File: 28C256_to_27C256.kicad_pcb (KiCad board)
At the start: 2 copper layers, 16.4 x 34.2 mm, 4 parts, among them J1 27C256 DIP LEGS, U1 28C256

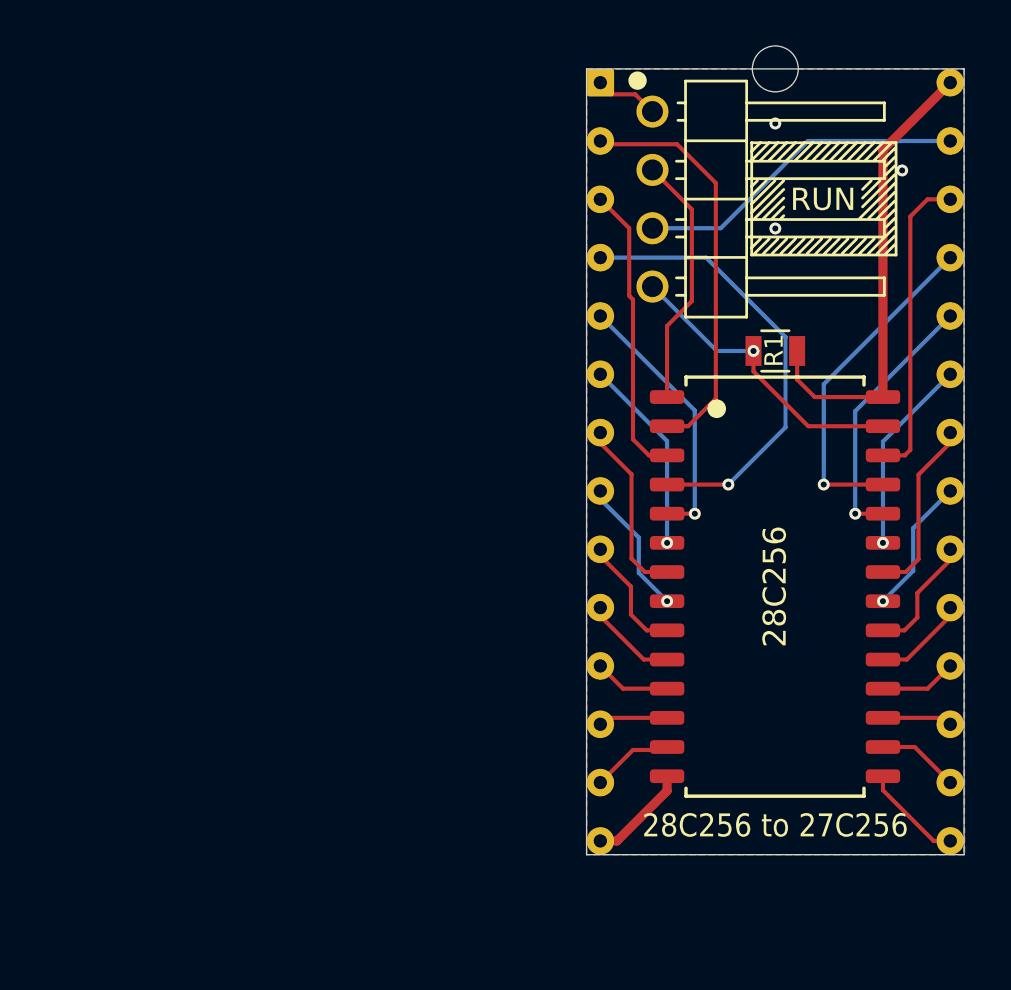
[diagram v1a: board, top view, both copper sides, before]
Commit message: simpler programming adapters, update pics and BOMs
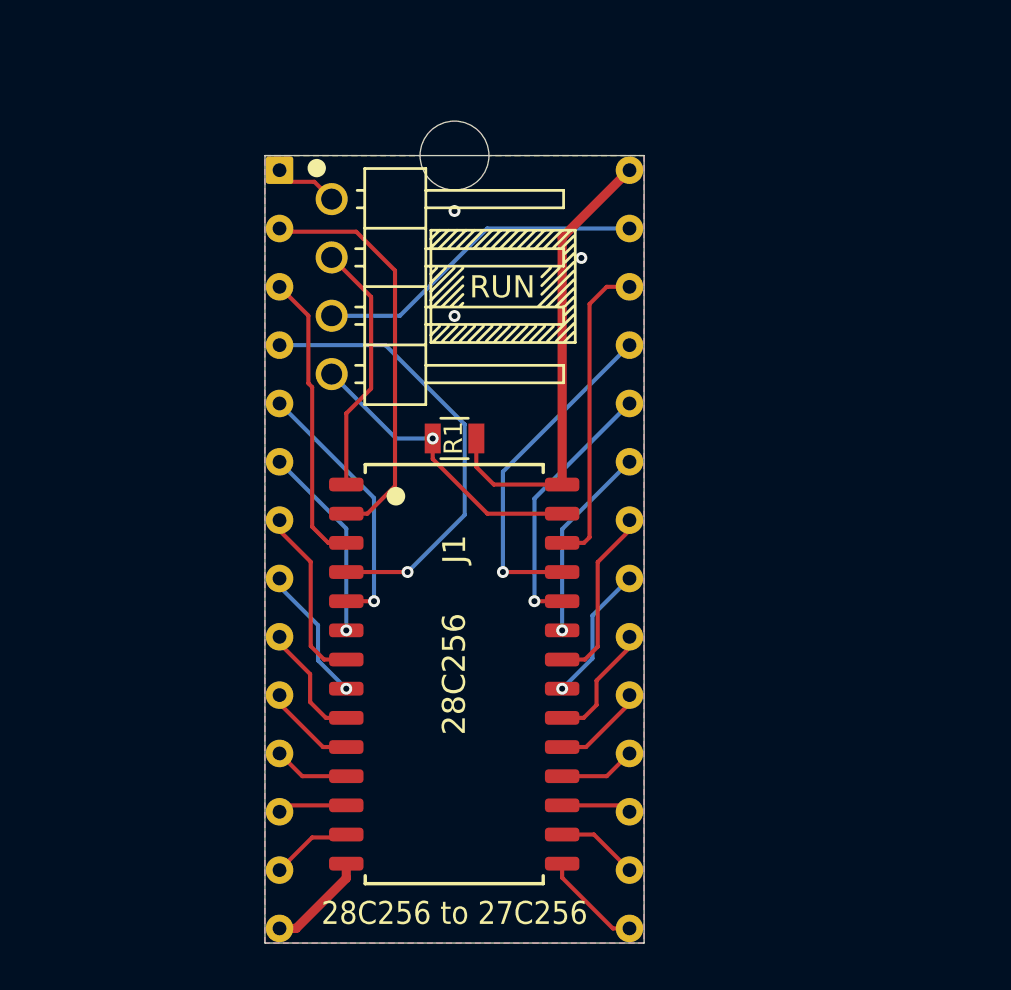
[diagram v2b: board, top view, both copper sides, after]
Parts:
- added REF**: NPTH_3mm, 000_LOCAL:NPTH_3mm, F.Cu at (136.0, 86.7)
- J1: footprint 000_LOCAL:DIP-28_W15.24mm_pcb_sil_pins -> 000_LOCAL:DIP28_0.6_pcb_sil_pins
- moved J1 14.5 mm to (136.0, 103.8)
- moved JP1 14.5 mm to (130.7, 88.6)
- moved U1 14.5 mm to (136.0, 109.2)
- moved R1 14.5 mm to (136.0, 99.0)
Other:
- board size 16.4 x 34.2 mm -> 16.5 x 34.3 mm

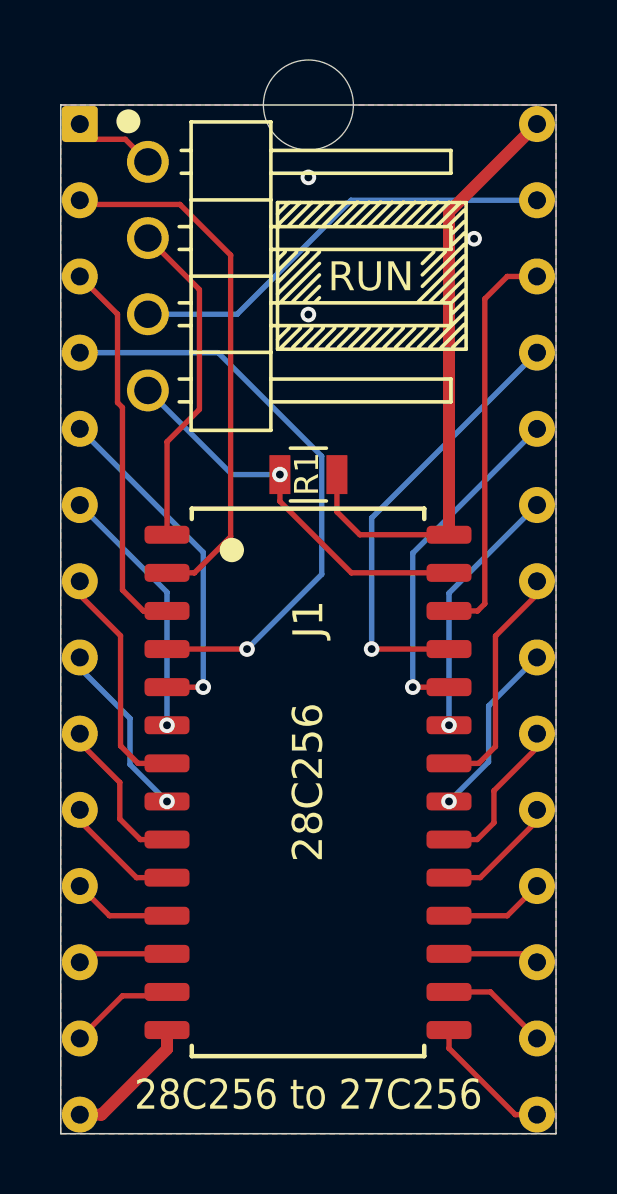
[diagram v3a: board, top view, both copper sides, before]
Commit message: 0.3mm drills, gnd zone fills
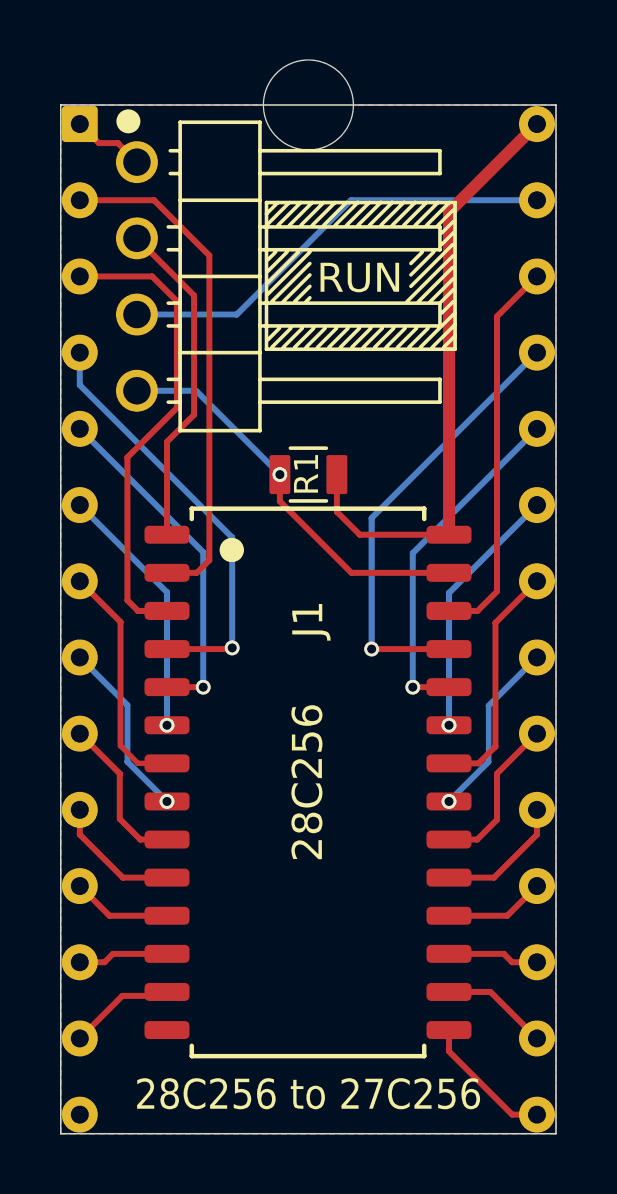
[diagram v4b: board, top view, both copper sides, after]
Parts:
- moved JP1 0.37 mm to (130.3, 88.6)
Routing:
- net /A6: track 19.6 -> 14.1 mm
- net /GND: track 4.45 -> 0.00 mm, vias 3 -> 0
- net /A7: track 12.8 -> 15.7 mm
- net /A12: track 17.8 -> 16.8 mm
- net /A13: track 13.5 -> 12.9 mm
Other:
- net class Default: trace_width 0.25 -> 0.2; via_dia 0.8 -> 0.5; via_drill 0.4 -> 0.3
- rule trace_min: 0.16 -> 0.2
- rule via_min_drill: 0.26 -> 0.3
- rule via_min_size: 0.52 -> 0.5

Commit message: make room to stow programming jumper on 28C256_to_27C256
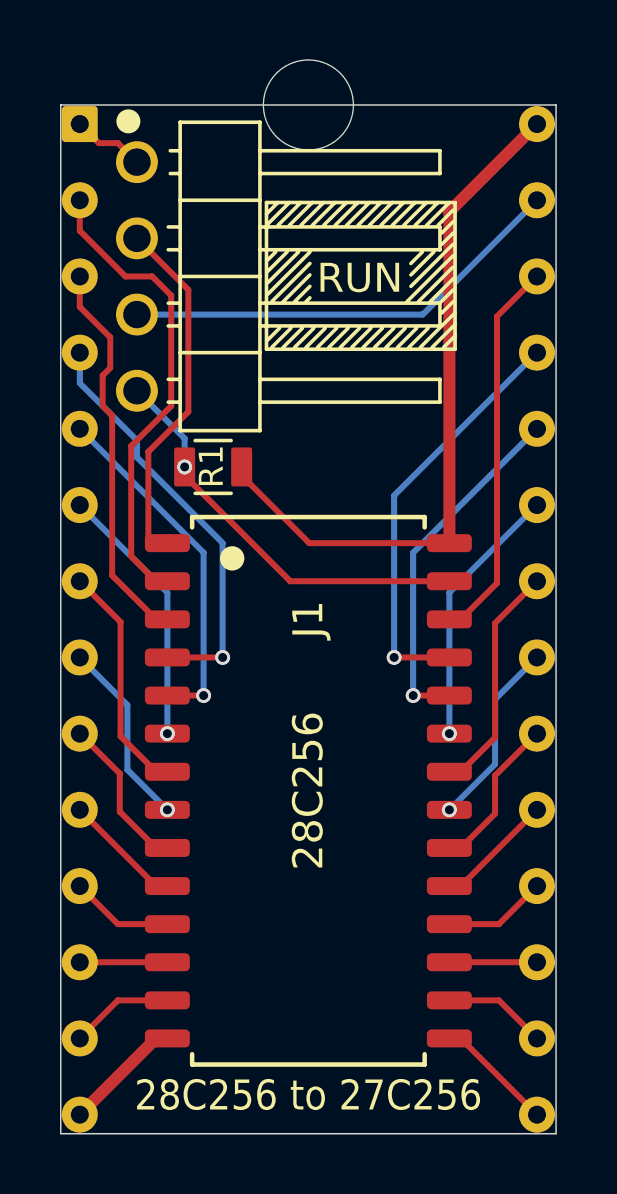
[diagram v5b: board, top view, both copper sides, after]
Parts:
- moved R1 3.19 mm to (132.9, 98.7)
- moved U1 0.28 mm to (136.0, 109.5)
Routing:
- net /GND: track 0.00 -> 3.97 mm
- net /VCC: track 20.2 -> 23.3 mm
- net /A7: track 15.7 -> 13.1 mm
- net /A12: track 16.8 -> 15.8 mm
- net /A14: track 11.0 -> 12.1 mm
- net /A8: track 14.7 -> 14.0 mm
- net /D3: track 4.52 -> 3.97 mm
- removed copper zone on B.Cu, net /GND
- removed copper zone on F.Cu, net /GND

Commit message: add DS1000_DIP14
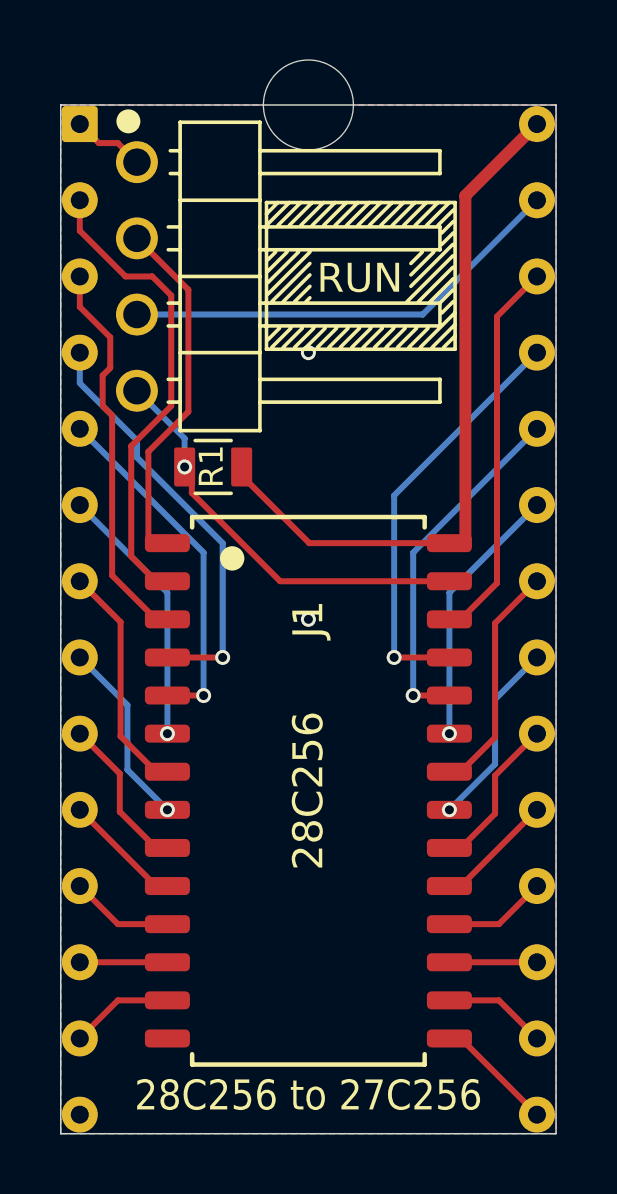
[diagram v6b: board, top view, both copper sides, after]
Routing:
- net /GND: track 3.97 -> 0.00 mm, vias 0 -> 2
- added copper zone on B.Cu, net /GND
- added copper zone on F.Cu, net /GND

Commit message: kicad 6
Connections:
- net /~CE renamed /~{CE}
- net /~OE renamed /~{OE}
- net /~WE renamed /~{WE}
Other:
- net class Default removed

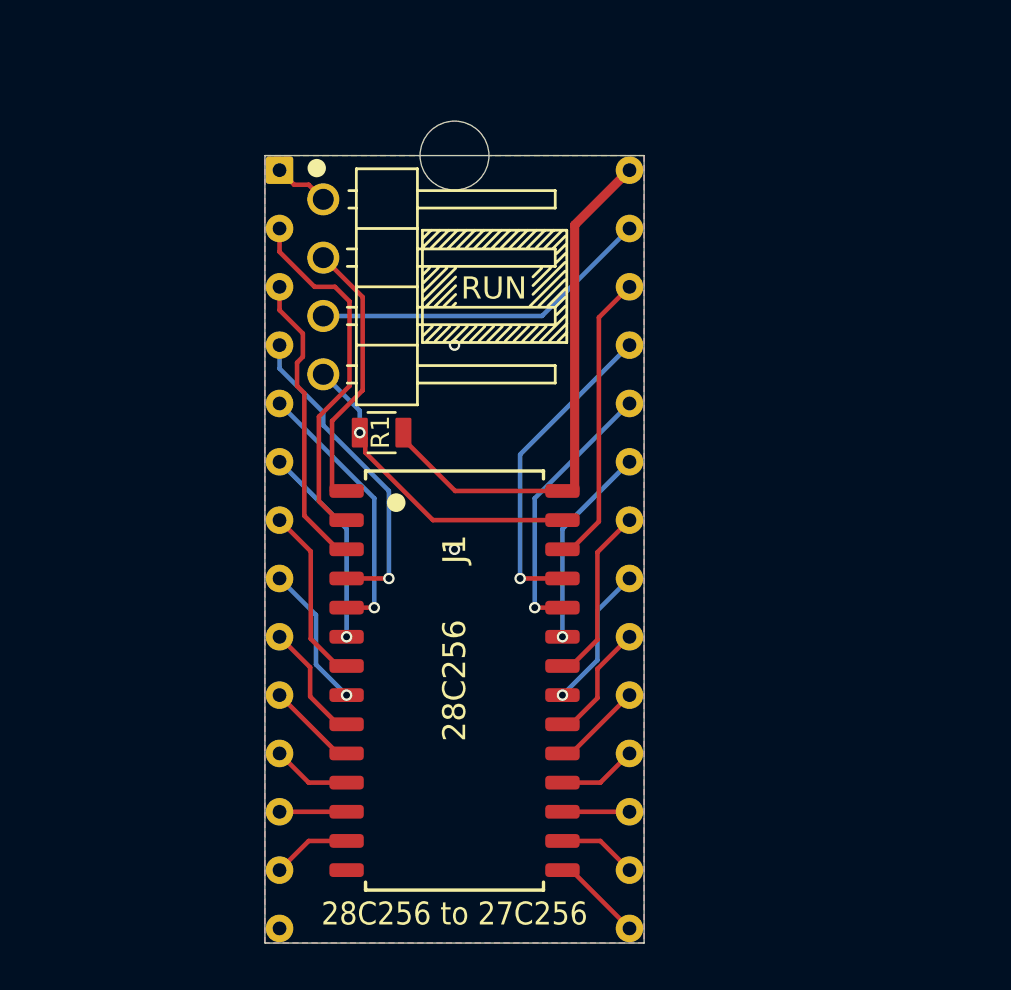
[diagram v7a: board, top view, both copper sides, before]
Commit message: Fix wrong pinout on FlashROM_100 TSOPgit add -A!
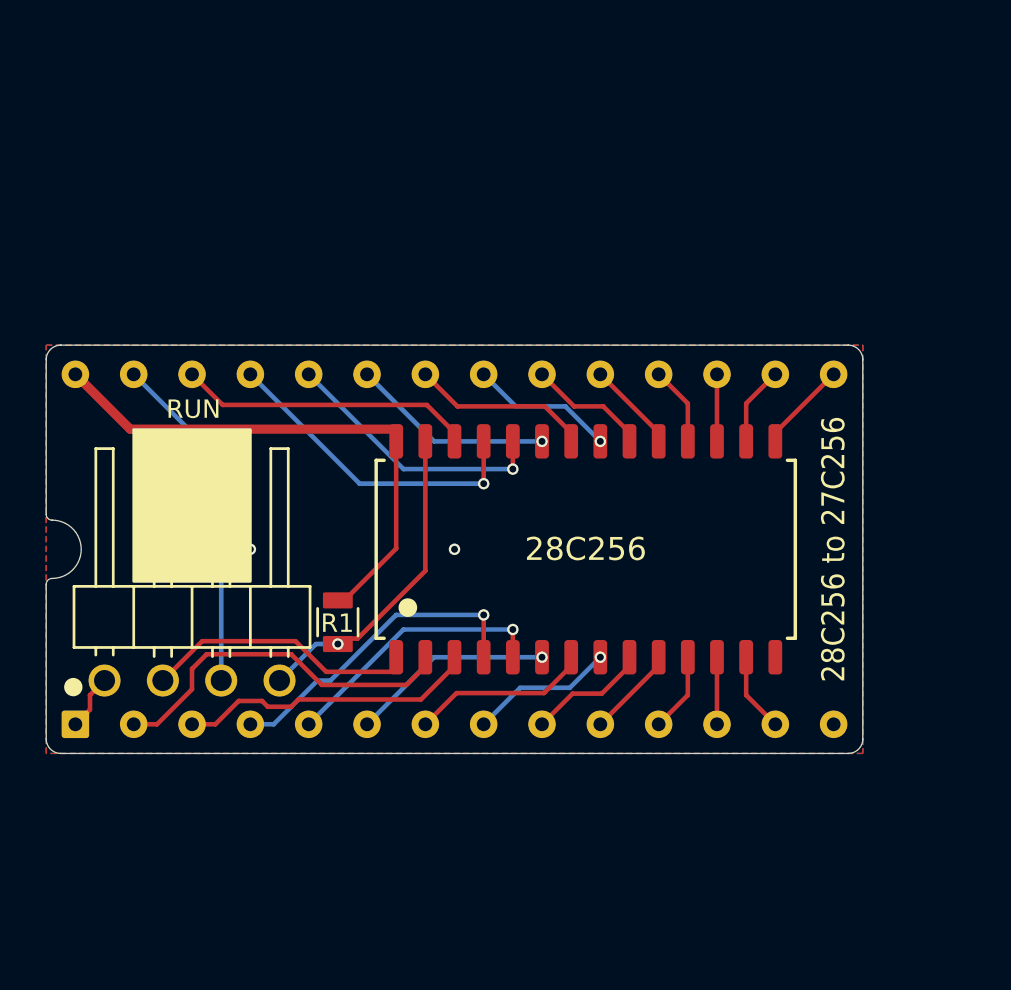
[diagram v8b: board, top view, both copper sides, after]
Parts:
- removed REF**: NPTH_3mm, 000_LOCAL:NPTH_3mm
- J1: footprint 000_LOCAL:DIP28_0.6_pcb_sil_pins -> 000_LOCAL:DIP28_0.6_pcb
- moved JP1 23.0 mm to (120.8, 109.5), turned to 90 degrees
- moved R1 8.47 mm to (130.9, 107.0), turned to 90 degrees
- moved U1 8.08 mm to (141.7, 103.8), turned to 90 degrees
- turned J1 to 90 degrees
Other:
- board size 16.5 x 34.3 mm -> 35.6 x 17.8 mm
- board text added: "27C256 pinout (RUN):"
- board text added: "28C256 pinout (PROGRAM):"
- board text added: "R1: ${00000000-0000-0000-0000-000060516c21:VALUE} Legs: TE 1544210"
- board text removed: "27C256 pinout (RUN)"
- board text removed: "28C256 pinout (PROGRAM)"
- board text removed: "Legs: TE 1544210"
- board text removed: "R1: 47k"
